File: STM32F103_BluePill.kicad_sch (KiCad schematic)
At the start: 28 parts, among them J1 USB_B_Micro, J2 Conn_01x04_Pin, J3 Conn_01x04_Pin, J4 Conn_01x04_Pin, SW1 SW_SPDT, U1 STM32F103C8T6, U2 AMS1117-3.3, Y1 16MHz

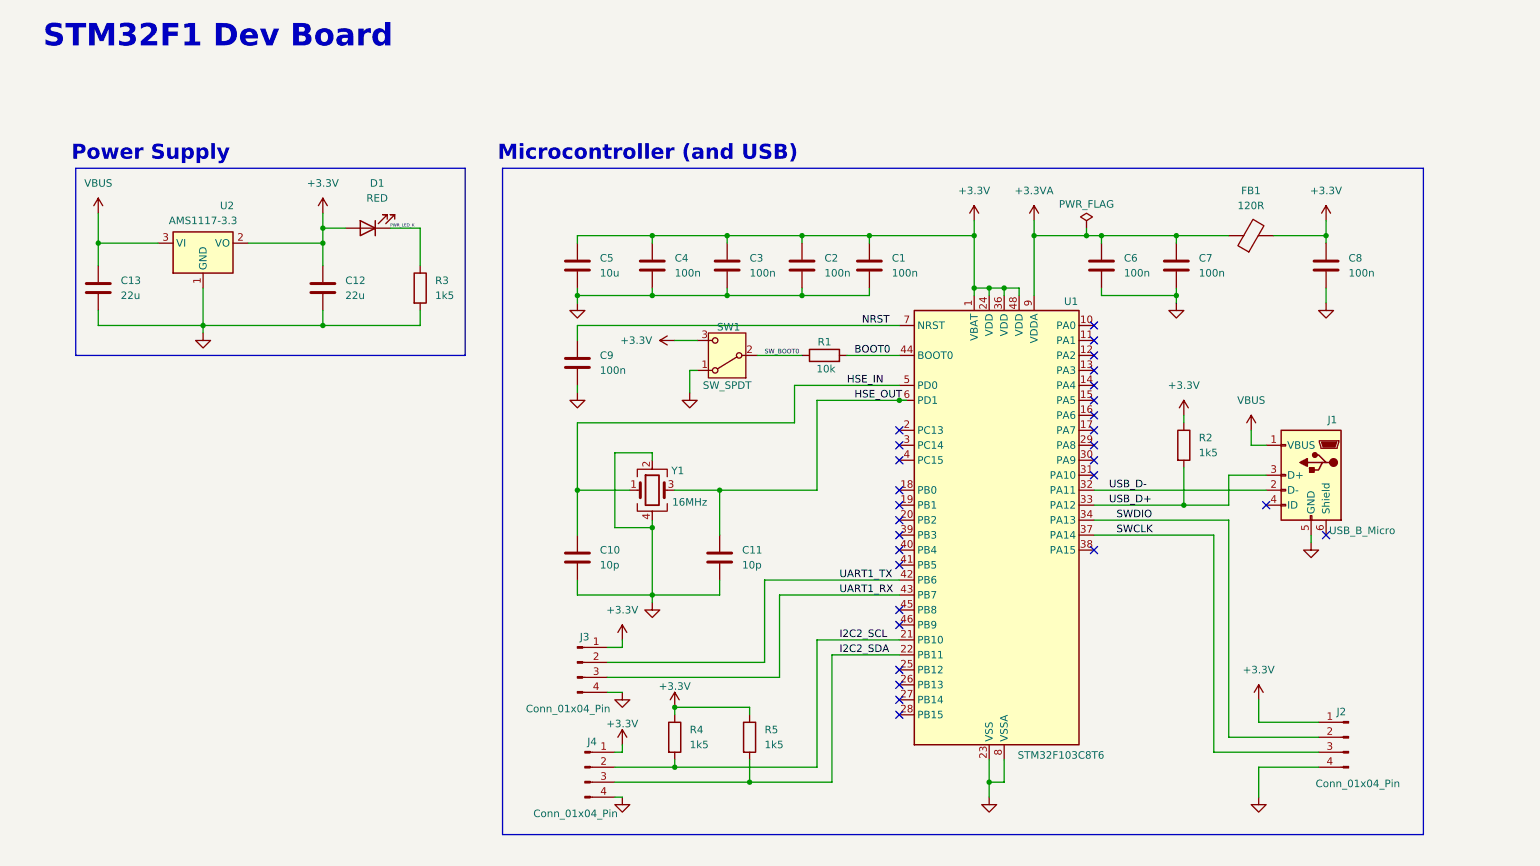
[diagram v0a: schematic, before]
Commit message: Completed PCB layout
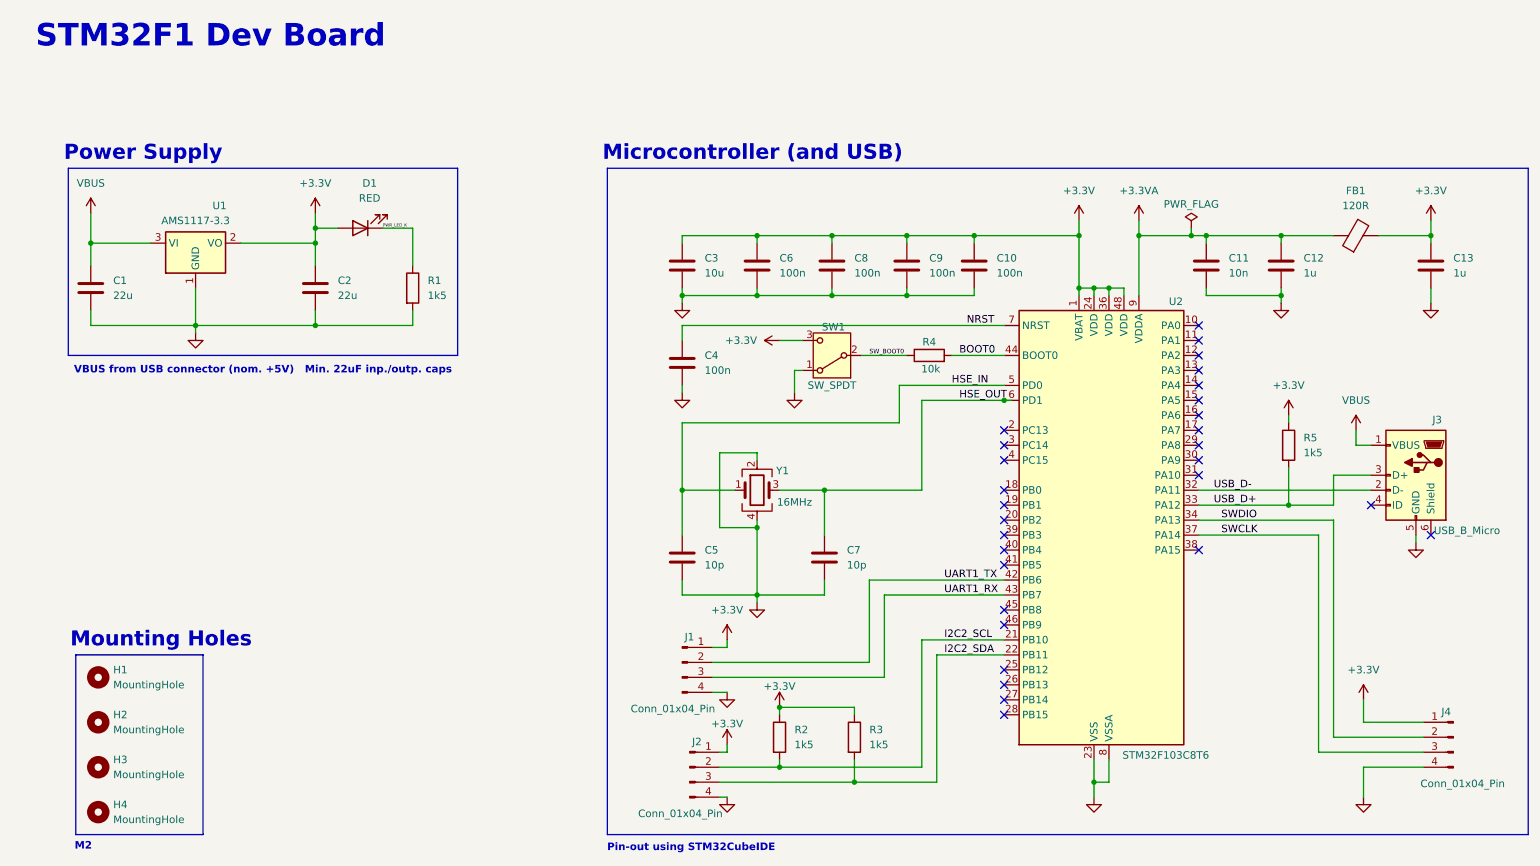
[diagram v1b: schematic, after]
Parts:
- removed J1: USB_B_Micro, symbol Connector:USB_B_Micro
- removed J3: Conn_01x04_Pin, symbol Connector:Conn_01x04_Pin
- removed U1: STM32F103C8T6, Package_QFP:LQFP-48_7x7mm_P0.5mm, symbol MCU_ST_STM32F1:STM32F103C8Tx
- removed U2: AMS1117-3.3, Package_TO_SOT_SMD:SOT-223-3_TabPin2, symbol Regulator_Linear:AMS1117-3.3
- added H1, H2, H3, H4: MountingHole, MountingHole:MountingHole_2.2mm_M2, symbol Mechanical:MountingHole
- added J1: Conn_01x04_Pin, Connector_PinHeader_2.54mm:PinHeader_1x04_P2.54mm_Vertical, symbol Connector:Conn_01x04_Pin
- added J3: USB_B_Micro, Connector_USB:USB_Micro-B_Wuerth_629105150521, symbol Connector:USB_B_Micro
- added U1: AMS1117-3.3, Package_TO_SOT_SMD:SOT-223-3_TabPin2, symbol Regulator_Linear:AMS1117-3.3
- added U2: STM32F103C8T6, Package_QFP:LQFP-48_7x7mm_P0.5mm, symbol MCU_ST_STM32F1:STM32F103C8Tx
- C1, C2: value 100n -> 22u; footprint (none) -> Capacitor_SMD:C_0805_2012Metric
- C10: value 10p -> 100n; footprint (none) -> Capacitor_SMD:C_0402_1005Metric
- C11: value 10p -> 10n; footprint (none) -> Capacitor_SMD:C_0402_1005Metric
- C12, C13: value 22u -> 1u; footprint (none) -> Capacitor_SMD:C_0402_1005Metric
- C3: value 100n -> 10u; footprint (none) -> Capacitor_SMD:C_0603_1608Metric
- C4, C6, C8, C9: footprint (none) -> Capacitor_SMD:C_0402_1005Metric
- C5: value 10u -> 10p; footprint (none) -> Capacitor_SMD:C_0402_1005Metric
- C7: value 100n -> 10p; footprint (none) -> Capacitor_SMD:C_0402_1005Metric
- D1: footprint (none) -> LED_SMD:LED_0603_1608Metric
- FB1: footprint (none) -> Inductor_SMD:L_0603_1608Metric
- J2, J4: footprint (none) -> Connector_PinHeader_2.54mm:PinHeader_1x04_P2.54mm_Vertical
- R1: value 10k -> 1k5; footprint (none) -> Resistor_SMD:R_0402_1005Metric
- R2, R3, R5: footprint (none) -> Resistor_SMD:R_0402_1005Metric
- R4: value 1k5 -> 10k; footprint (none) -> Resistor_SMD:R_0402_1005Metric
- SW1: footprint (none) -> Button_Switch_SMD:SW_SPDT_PCM12
- Y1: footprint (none) -> Crystal:Crystal_SMD_3225-4Pin_3.2x2.5mm
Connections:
- net +3.3V: now also C10.1, C13.1, C6.1, C9.1, R3.1, J1.1 (Pin_1), U1.2 (VO), U2.1 (VBAT), U2.24 (VDD), U2.36 (VDD), U2.48 (VDD); no longer C1.1, C12.1, C4.1, C5.1, R4.1
- net +3.3VA: now also C11.1, C12.1, U2.9 (VDDA); no longer C6.1, C7.1
- net BOOT0: now also R4.2, U2.44 (BOOT0); no longer R1.2
- net GND: now also R1.2, J1.4 (Pin_4), J3.5 (GND), U1.1 (GND), U2.23 (VSS), U2.35 (VSS), U2.47 (VSS), U2.8 (VSSA); no longer R3.2
- net HSE_IN: now also C5.1, U2.5 (PD0); no longer C10.1
- net HSE_OUT: now also C7.1, U2.6 (PD1); no longer C11.1
- net I2C2_SCL: now also J2.2 (Pin_2), R2.2, U2.21 (PB10); no longer J4.2 (Pin_2), R4.2
- net I2C2_SDA: now also J2.3 (Pin_3), R3.2, U2.22 (PB11); no longer J4.3 (Pin_3), R5.2
- net NRST: now also C4.1, U2.7 (NRST); no longer C9.1
- net PWR_LED_K: now also R1.1; no longer R3.1
- net SWCLK: now also J4.3 (Pin_3), U2.37 (PA14); no longer J2.3 (Pin_3)
- net SWDIO: now also J4.2 (Pin_2), U2.34 (PA13); no longer J2.2 (Pin_2)
- net SW_BOOT0: now also R4.1; no longer R1.1
- net UART1_RX: now also J1.3 (Pin_3), U2.43 (PB7)
- net UART1_TX: now also J1.2 (Pin_2), U2.42 (PB6)
- net USB_D+: now also R5.2, J3.3 (D+), U2.33 (PA12); no longer R2.2
- net USB_D-: now also J3.2 (D-), U2.32 (PA11)
- net VBUS: now also C1.1, J3.1 (VBUS), U1.3 (VI); no longer C13.1
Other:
- note added: "M2"
- note added: "Mounting Holes"
- note added: "Pin-out using STM32CubeIDE"
- note added: "VBUS from USB connector (nom. +5V) Min. 22uF inp./outp. caps"
